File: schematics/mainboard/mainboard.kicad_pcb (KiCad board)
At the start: 2 copper layers, 166.4 x 91.4 mm, 22 parts, among them J1 ICSP, J2 USB_B_Micro, J3 Jack-DC, J4 PWR_SELECT, U1 ATmega2560-16A, U2 FT232RL, Y1 16Mhz

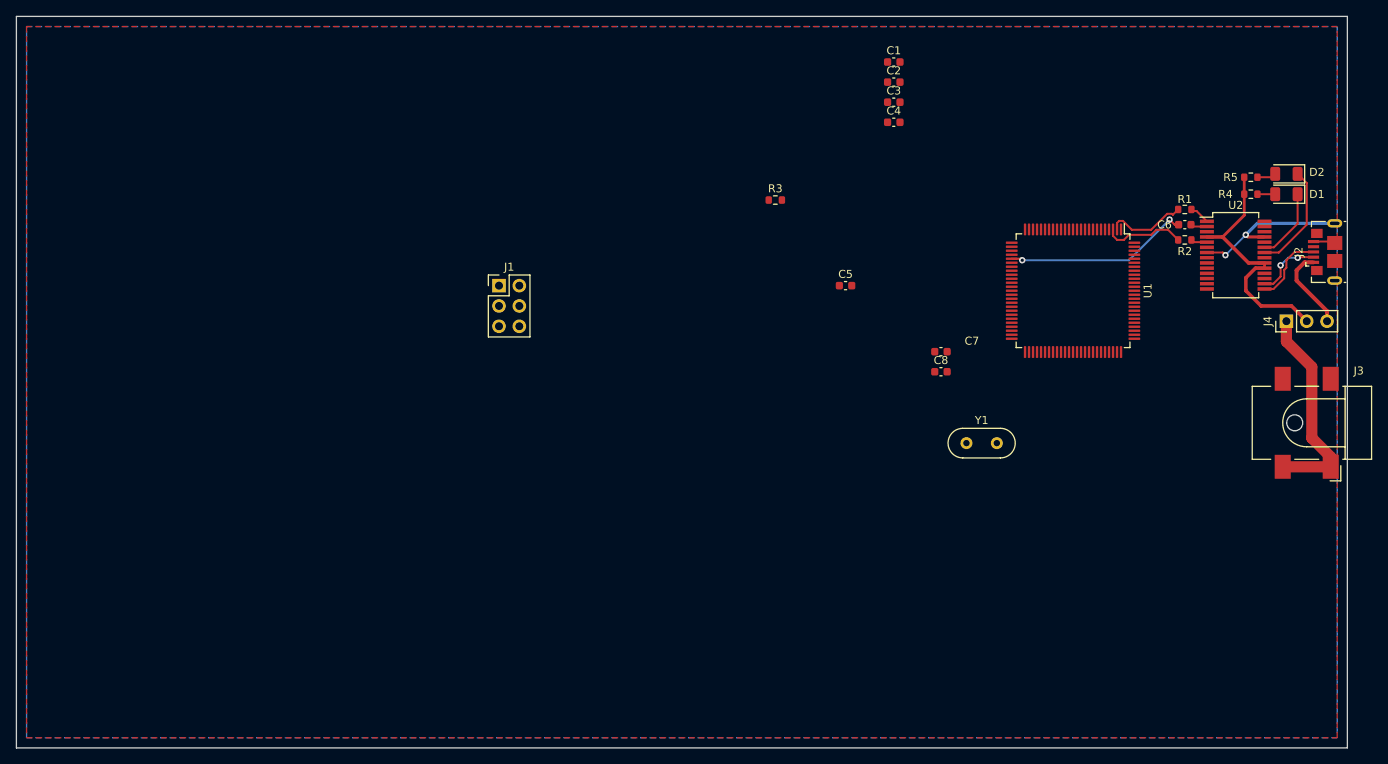
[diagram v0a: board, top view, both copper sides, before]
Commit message: SCH: mainboard: cont.
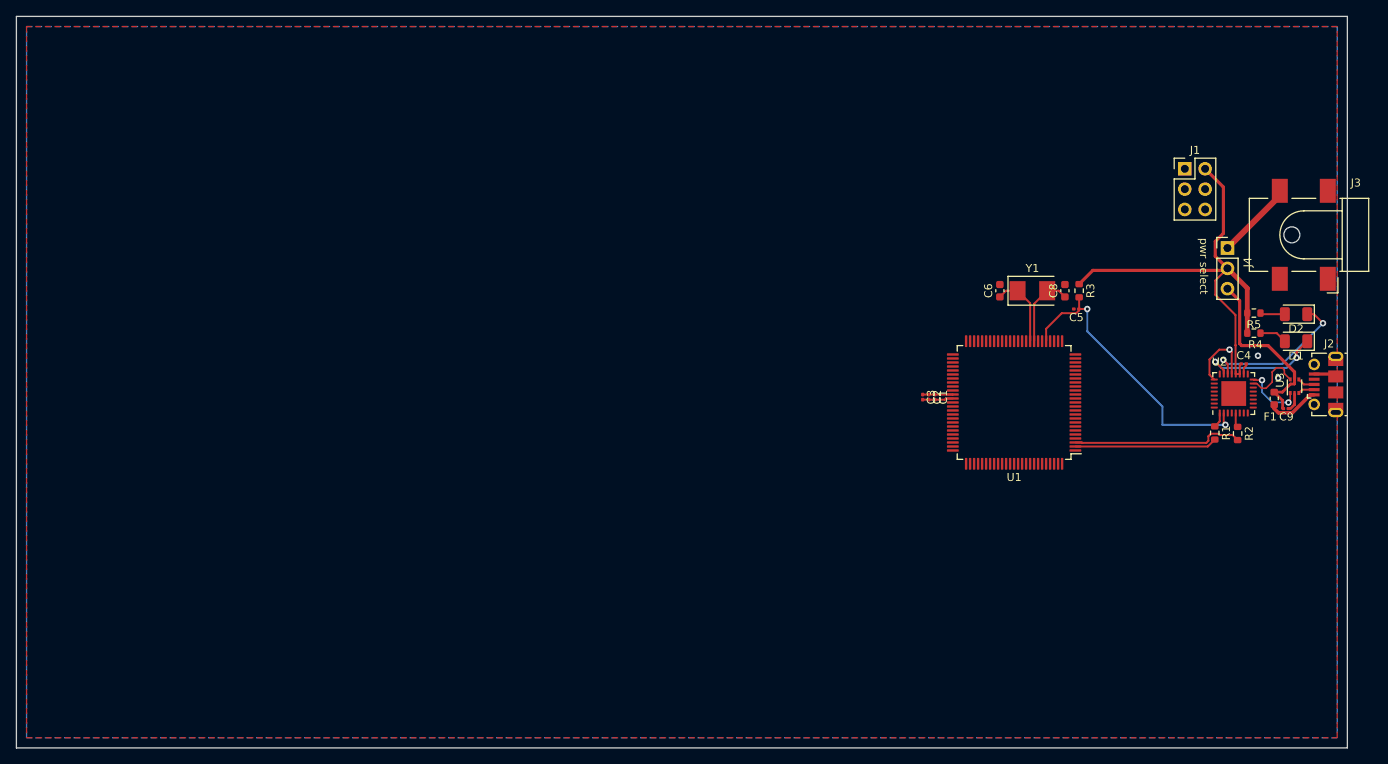
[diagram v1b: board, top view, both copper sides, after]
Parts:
- removed C7: 22pF, Capacitor_SMD:C_0603_1608Metric
- added C9: 100nF, Capacitor_SMD:C_0201_0603Metric, F.Cu at (196.8, 70.6)
- added F1: 500mA Poly, Fuse:Fuse_0603_1608Metric, F.Cu at (195.3, 69.3)
- added U3: USBLC6-2P6, Package_TO_SOT_SMD:SOT-666, F.Cu at (197.9, 67.8)
- C1, C2, C3: footprint Capacitor_SMD:C_0603_1608Metric -> Capacitor_SMD:C_0201_0603Metric
- C4, C5: value 0.1uF -> 100nF; footprint Capacitor_SMD:C_0603_1608Metric -> Capacitor_SMD:C_0201_0603Metric
- C6: value 0.1uF -> 22pF
- J2: footprint Connector_USB:USB_Micro-B_GCT_USB3076-30-A -> Connector_USB:USB_Micro-B_Molex-105017-0001
- J3: value Jack-DC -> DEALON DC-S050-200
- U2: footprint Package_SO:SSOP-28_5.3x10.2mm_P0.65mm -> Package_DFN_QFN:HVQFN-32-1EP_5x5mm_P0.5mm_EP3.1x3.1mm
- Y1: footprint Crystal:Crystal_HC52-8mm_Vertical -> Crystal:Crystal_SMD_5032-2Pin_5.0x3.2mm
- moved J1 87.0 mm to (184.2, 40.6)
- moved C4 53.2 mm to (191.5, 65.0)
- moved C1 42.2 mm to (152.9, 69.2), turned to -90 degrees
- moved R3 39.6 mm to (170.9, 55.9), turned to -90 degrees
- moved C2 39.6 mm to (152.1, 69.2), turned to -90 degrees
- moved C3 37.0 mm to (151.4, 69.2), turned to -90 degrees
- moved C5 29.0 mm to (170.6, 58.2), turned to 180 degrees
- moved R1 28.2 mm to (187.9, 73.7), turned to -90 degrees
- moved R2 25.1 mm to (190.8, 73.7), turned to -90 degrees
- moved C6 24.5 mm to (161.0, 55.9), turned to 90 degrees
- moved J3 23.5 mm to (199.0, 48.9)
- moved Y1 20.8 mm to (165.1, 55.9)
- moved C8 18.5 mm to (169.2, 55.9), turned to 90 degrees
- moved D1 18.4 mm to (198.1, 62.2)
- moved D2 17.6 mm to (198.1, 58.8)
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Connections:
- net Net-(U1-PE0) renamed /FTDI_TX
- net Net-(U1-PE1) renamed /FTDI_RX
- C6 pad 1: /RESET -> Net-(U1-XTAL1)
- C6 pad 2: /DTR -> GND
- J3 pad 1: Net-(J4-Pin_1) -> GND
- J3 pad 2: GND -> Net-(J4-Pin_1)
- J3 pad 3: (no net) -> unconnected-(J3-Pad3)
- J4 pad 3: Net-(J2-VBUS) -> Net-(J4-Pin_3)
- U2 pad 15: Net-(J2-D+) -> /D+
- U2 pad 16: Net-(J2-D-) -> /D-
- U2 pad 2: /DTR -> /RESET
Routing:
- net +5V: track 31.4 -> 63.4 mm
- net Net-(J4-Pin_3): track 0.00 -> 22.8 mm
- net Net-(J4-Pin_1): track 26.5 -> 9.86 mm
- net /RESET: track 23.3 -> 37.4 mm
- net /FTDI_RX: track 10.2 -> 21.4 mm
- net Net-(U1-XTAL1): track 0.00 -> 10.2 mm
- net Net-(U1-XTAL2): track 0.00 -> 9.52 mm
- net /D-: track 0.00 -> 7.76 mm, vias 0 -> 2
- net /FTDI_TX: track 10.2 -> 17.8 mm
- net /D+: track 0.00 -> 7.52 mm
- net Net-(J2-D+): track 9.20 -> 2.18 mm
- net Net-(D1-K): track 9.04 -> 15.6 mm, vias 0 -> 2
- net Net-(J2-D-): track 8.32 -> 2.09 mm, vias 2 -> 0
- net GND: track 22.9 -> 17.0 mm, vias 2 -> 3
- net Net-(D2-K): track 13.5 -> 19.2 mm, vias 0 -> 2
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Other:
- board text added: "pwr select"

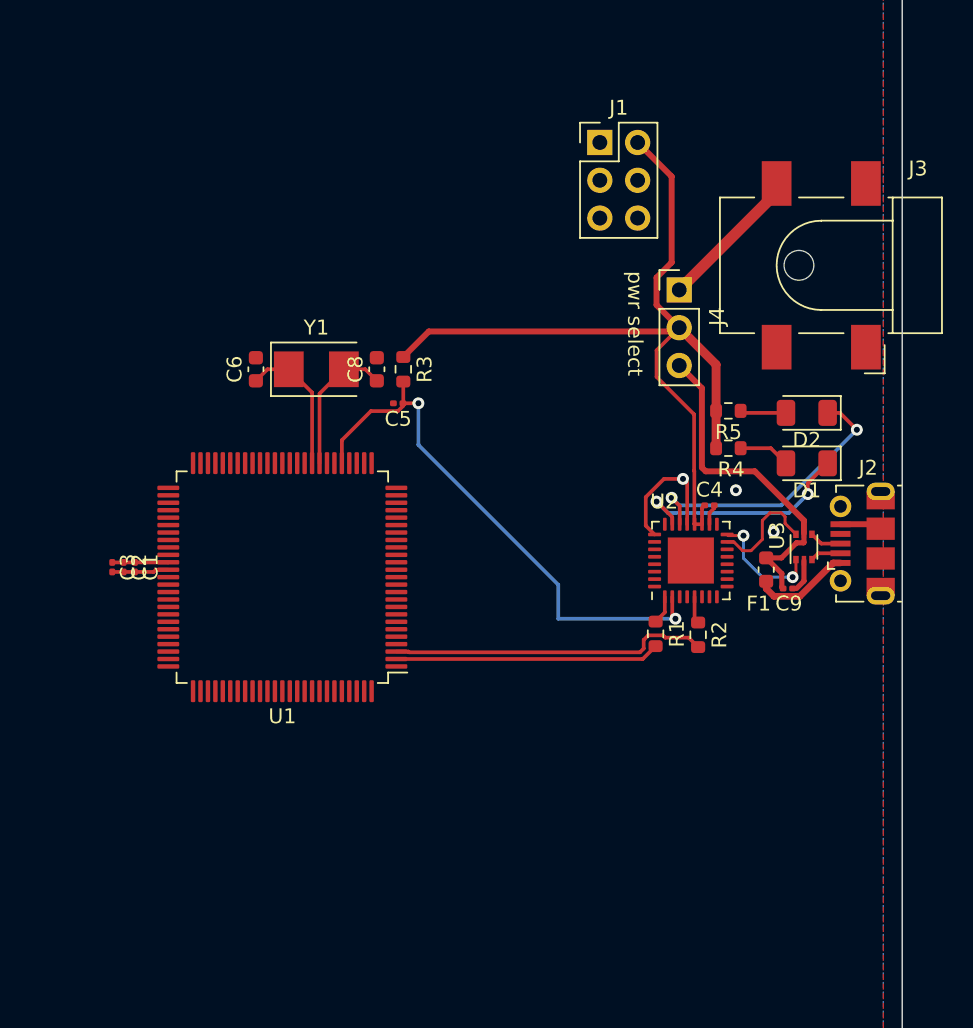
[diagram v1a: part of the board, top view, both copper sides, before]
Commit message: SCH: mainboard=> +regu on VIN. routing cont.
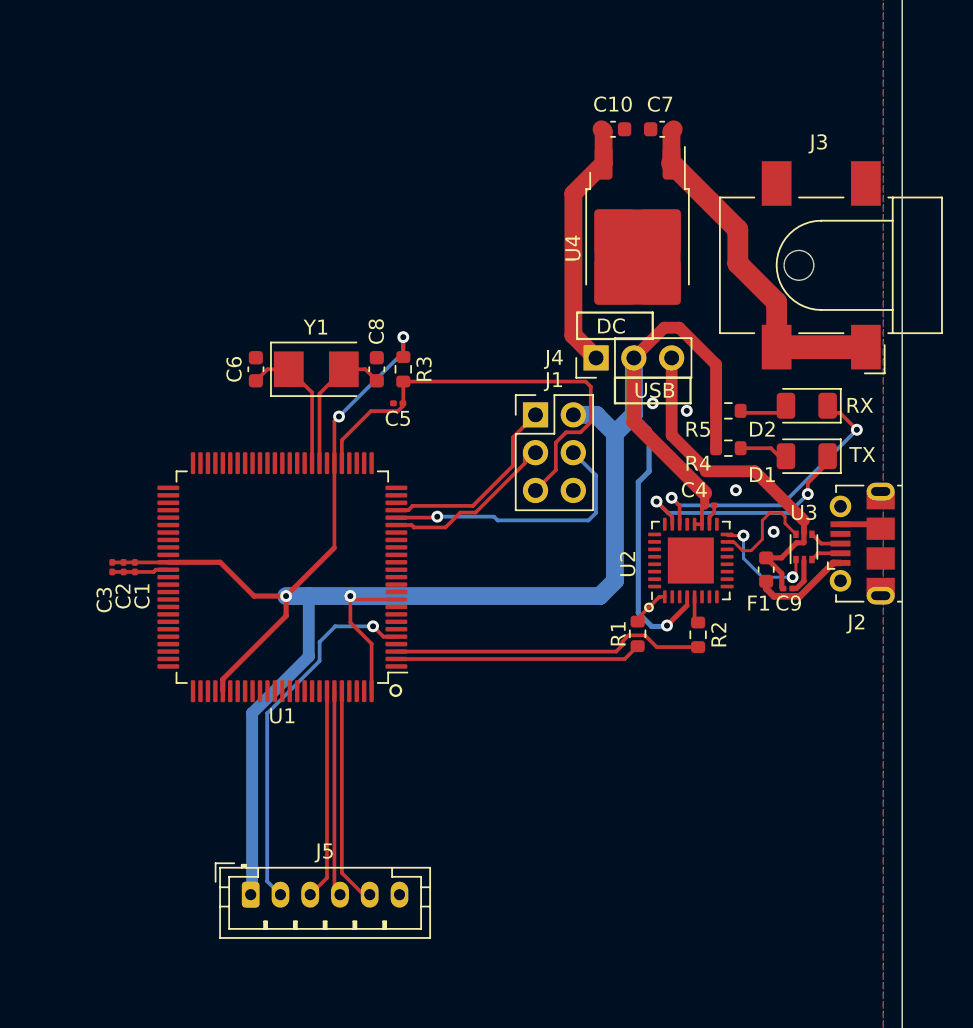
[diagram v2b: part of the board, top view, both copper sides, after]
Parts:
- added C10: 100nF, Capacitor_SMD:C_0603_1608Metric, F.Cu at (185.0, 39.8)
- added C7: 330nF, Capacitor_SMD:C_0603_1608Metric, F.Cu at (188.3, 39.8)
- added J5: JOY1, Connector_JST:JST_PH_B6B-PH-K_1x06_P2.00mm_Vertical, F.Cu at (160.7, 91.2)
- added U4: AIP78M05, Package_TO_SOT_SMD:TO-252-2, F.Cu at (186.7, 47.1)
- C5: value 100nF -> 0.1uF
- moved J1 18.8 mm to (179.8, 58.9)
- moved J4 7.22 mm to (183.9, 55.1), turned to 90 degrees
- moved R1 1.21 mm to (186.7, 73.7)
- moved D1 0.48 mm to (198.1, 61.7)
- moved D2 0.48 mm to (198.1, 58.3)
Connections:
- J3 pad 1: GND -> VDD
- J3 pad 2: Net-(J4-Pin_1) -> GND
- U1 pad 5: unconnected-(U1-PE3-Pad5) -> Net-(J5-Pin_2)
- U1 pad 94: unconnected-(U1-PF3-Pad94) -> Net-(J5-Pin_3)
- U1 pad 95: unconnected-(U1-PF2-Pad95) -> Net-(J5-Pin_4)
- U1 pad 96: unconnected-(U1-PF1-Pad96) -> Net-(J5-Pin_5)
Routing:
- net +5V: track 63.4 -> 161.6 mm, vias 0 -> 5
- net Net-(J5-Pin_2): track 0.00 -> 24.7 mm, vias 0 -> 1
- net VDD: track 0.00 -> 23.6 mm
- net /MOSI: track 0.00 -> 18.4 mm, vias 0 -> 1
- net Net-(J5-Pin_5): track 0.00 -> 14.7 mm
- net Net-(J5-Pin_3): track 0.00 -> 14.1 mm
- net Net-(J5-Pin_4): track 0.00 -> 13.8 mm
- net /MISO: track 0.00 -> 13.1 mm
- net /SCK: track 0.00 -> 11.9 mm
- net GND: track 17.0 -> 7.63 mm, vias 3 -> 4
- net /RESET: track 37.4 -> 30.0 mm, vias 2 -> 0
- net Net-(J4-Pin_1): track 9.86 -> 16.9 mm
- net /FTDI_TX: track 17.8 -> 16.6 mm
- net Net-(J4-Pin_3): track 22.8 -> 23.5 mm
- net Net-(U1-XTAL1): track 10.2 -> 9.49 mm
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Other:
- board text added: "DC"
- board text added: "RX"
- board text added: "TX"
- board text added: "USB"
- board text removed: "pwr select"

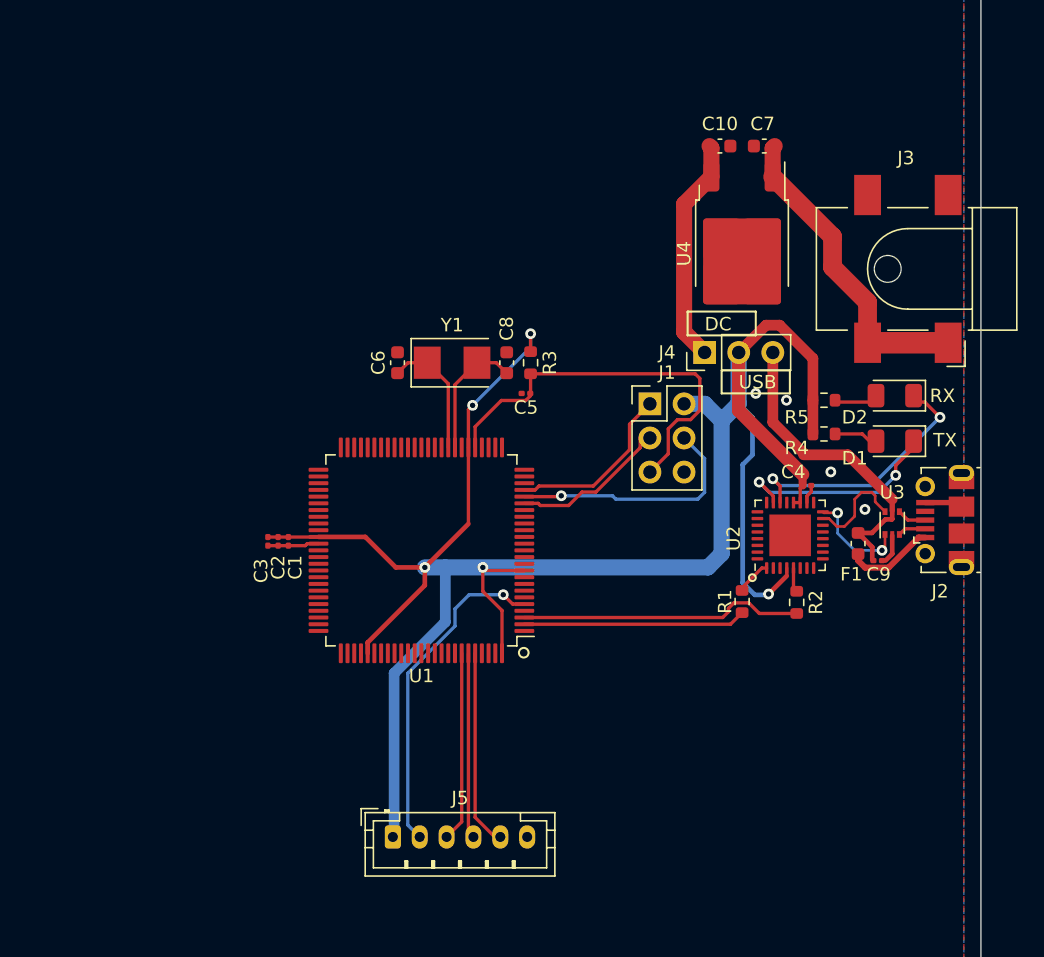
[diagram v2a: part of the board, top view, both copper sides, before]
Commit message: SCH: mainboard=> joy2 header + throttle header
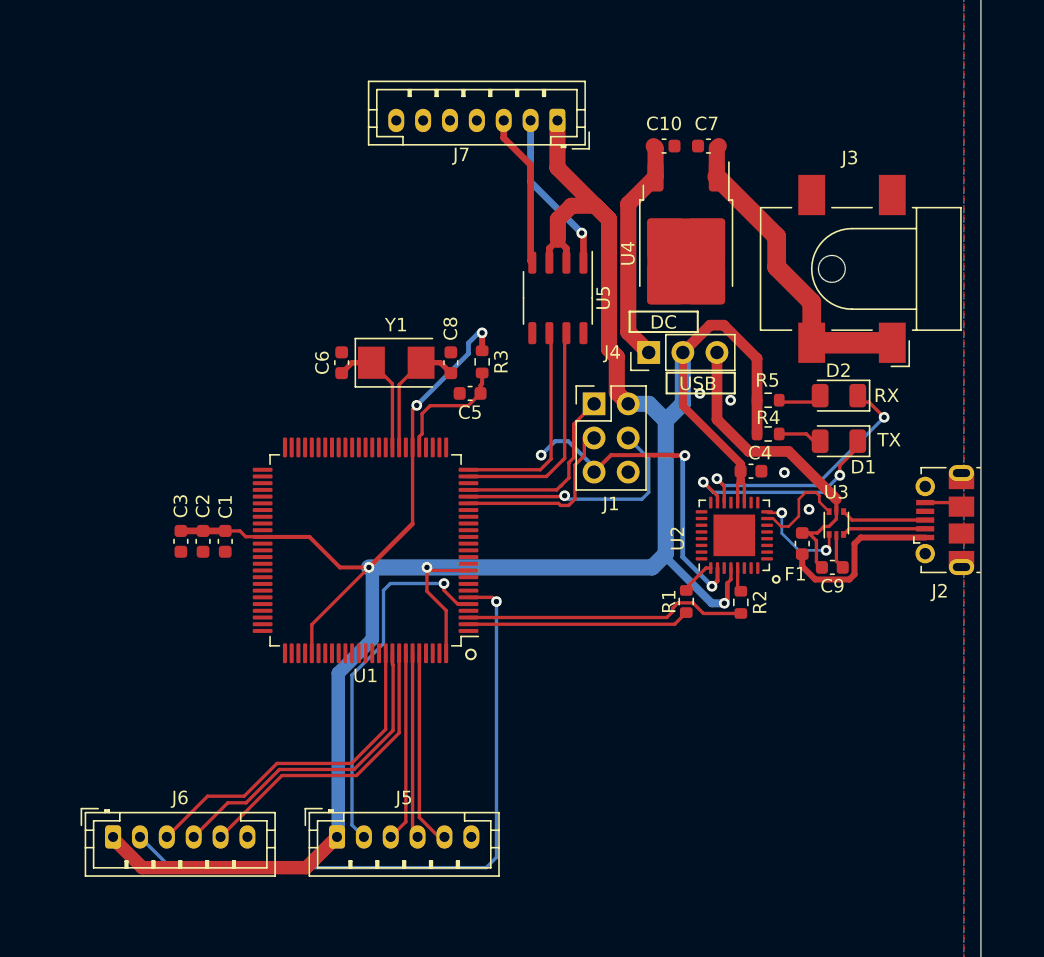
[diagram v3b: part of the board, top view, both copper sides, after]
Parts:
- added J6: JOY2, Connector_JST:JST_PH_B6B-PH-K_1x06_P2.00mm_Vertical, F.Cu at (139.9, 91.2)
- added J7: Throttle, Connector_JST:JST_PH_B7B-PH-K_1x07_P2.00mm_Vertical, F.Cu at (172.9, 37.8)
- added U5: L9110, Package_SO:SOP-8_3.9x4.9mm_P1.27mm, F.Cu at (173.0, 51.1)
- C1, C2, C3, C4, C5, C9: footprint Capacitor_SMD:C_0201_0603Metric -> Capacitor_SMD:C_0603_1608Metric
- moved C3 6.48 mm to (144.9, 69.2)
- moved C2 5.59 mm to (146.6, 69.2)
- moved C1 4.70 mm to (148.2, 69.2)
- moved C4 4.30 mm to (187.4, 64.0)
- moved C5 4.16 mm to (166.4, 58.2)
- moved C6 4.16 mm to (156.9, 55.9)
- moved C7 4.16 mm to (184.2, 39.8)
- moved R4 4.16 mm to (188.6, 61.2)
- moved R5 4.16 mm to (188.6, 58.7)
- moved U3 4.16 mm to (193.7, 67.8)
- moved C10 4.16 mm to (180.9, 39.8)
- moved C8 4.16 mm to (165.0, 55.9)
- moved D1 4.16 mm to (193.9, 61.7)
- moved D2 4.16 mm to (193.9, 58.3)
- moved F1 4.16 mm to (191.2, 69.3)
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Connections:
- U1 pad 12: unconnected-(U1-PH0-Pad12) -> Net-(J7-Pin_4)
- U1 pad 13: unconnected-(U1-PH1-Pad13) -> Net-(J7-Pin_5)
- U1 pad 24: unconnected-(U1-PB5-Pad24) -> /THROTTLE_UP
- U1 pad 25: unconnected-(U1-PB6-Pad25) -> /THROTTLE_DOWN
- U1 pad 6: unconnected-(U1-PE4-Pad6) -> Net-(J6-Pin_2)
- U1 pad 90: unconnected-(U1-PF7-Pad90) -> Net-(J7-Pin_6)
- U1 pad 91: unconnected-(U1-PF6-Pad91) -> Net-(J6-Pin_3)
- U1 pad 92: unconnected-(U1-PF5-Pad92) -> Net-(J6-Pin_4)
- U1 pad 93: unconnected-(U1-PF4-Pad93) -> Net-(J6-Pin_5)
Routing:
- net Net-(J6-Pin_2): track 0.00 -> 49.1 mm, vias 0 -> 1
- net +5V: track 161.6 -> 207.2 mm
- net Net-(J6-Pin_3): track 0.00 -> 25.3 mm
- net Net-(J6-Pin_4): track 0.00 -> 23.9 mm
- net Net-(J6-Pin_5): track 0.00 -> 22.4 mm
- net /THROTTLE_UP: track 0.00 -> 17.1 mm
- net /THROTTLE_DOWN: track 0.00 -> 15.9 mm
- net Net-(J7-Pin_2): track 0.00 -> 12.2 mm, vias 0 -> 1
- net Net-(J7-Pin_3): track 0.00 -> 11.5 mm
- net Net-(J2-VBUS): track 6.63 -> 13.1 mm
- net GND: track 7.63 -> 2.82 mm
- net /RESET: track 30.0 -> 34.2 mm, vias 0 -> 3
- net Net-(J2-D+): track 2.18 -> 6.34 mm
- net Net-(J2-D-): track 2.09 -> 6.25 mm
- net Net-(J5-Pin_2): track 24.7 -> 27.2 mm
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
